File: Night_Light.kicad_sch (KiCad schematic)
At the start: 6 parts, among them J1 3V0, Q1 2N3904

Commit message: Update schematic for KiCad version 7
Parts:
- J1: symbol Connector:Conn_01x02_Male -> Connector:Conn_01x02_Pin

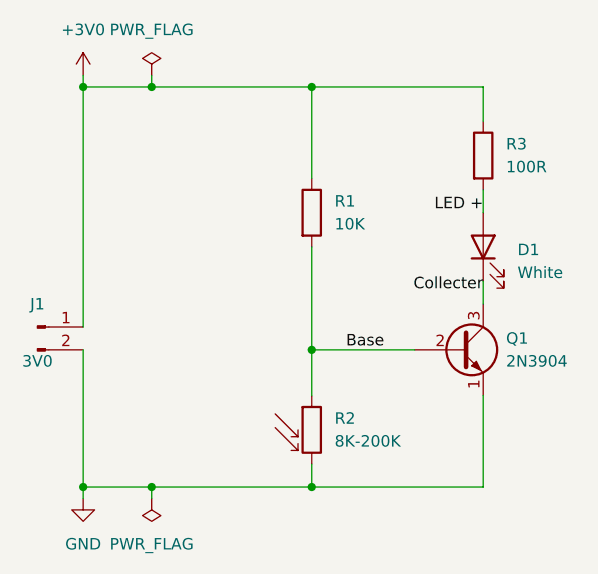
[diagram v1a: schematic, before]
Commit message: Update silkscreen. Fixes #7, #8, #9, and #11
- Change "D1" label to "LED1". #7
- Make silkscreen text bigger and thicker. #8
- Add "+" and "-" to power pads. #9
- Add LED polarity to silkscreen. #11
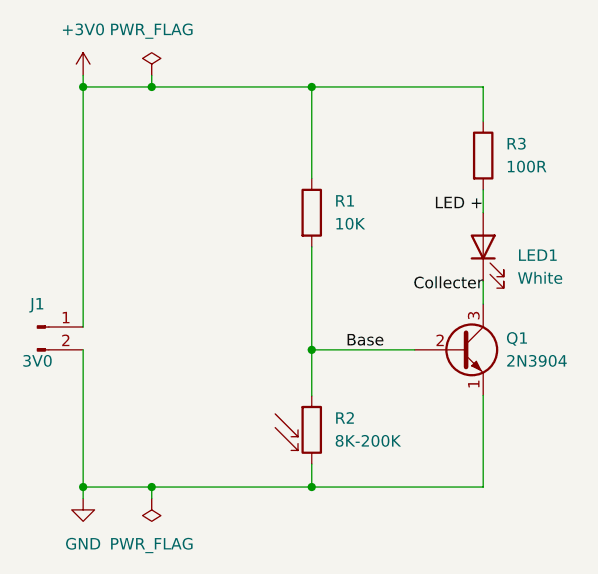
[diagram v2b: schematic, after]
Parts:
- renumbered D1 to LED1
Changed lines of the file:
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@@
   (symbol (lib_id "Device:LED") (at 158.75 93.98 90) (unit 1)
     (in_bom yes) (on_board yes) (dnp no) (fields_autoplaced)
-    (property "Reference" "D1" (at 162.56 94.2974 90)
+    (property "Reference" "LED1" (at 162.56 94.9325 90)
       (effects (font (size 1.27 1.27)) (justify right))
     )
-    (property "Value" "White" (at 162.56 96.8374 90)
+    (property "Value" "White" (at 162.56 97.4725 90)
       (effects (font (size 1.27 1.27)) (justify right))
     )
@@
       (project "Night_Light"
         (path "/92c86926-e096-47bb-9196-37834700b996"
-          (reference "D1") (unit 1)
+          (reference "LED1") (unit 1)
         )
       )

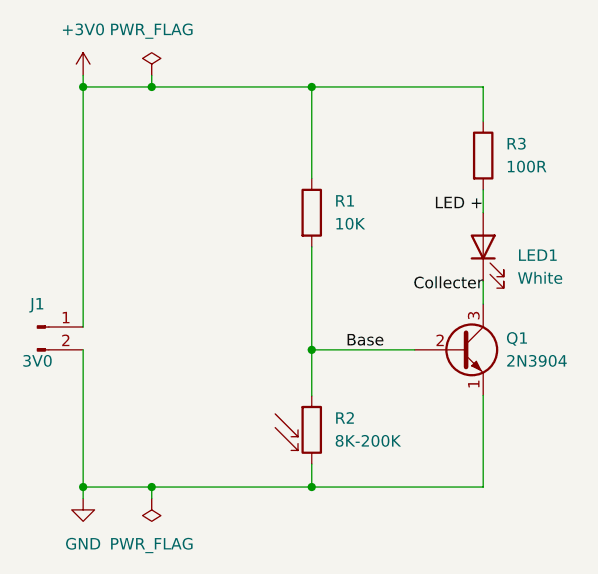
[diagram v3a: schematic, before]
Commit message: Change R3 and add resistor values to silkscreen
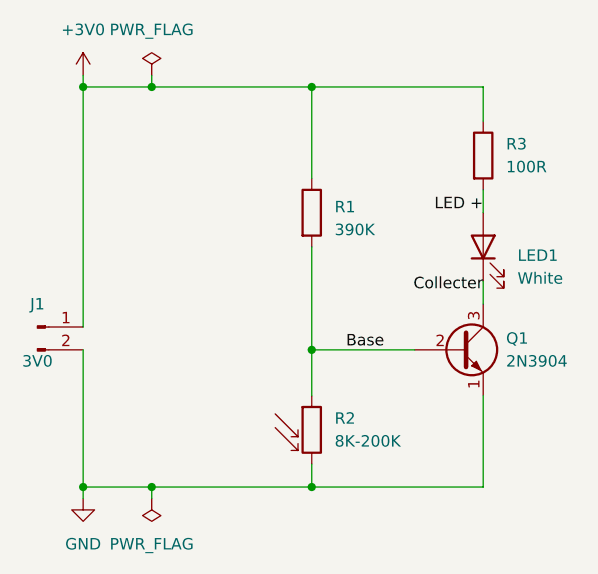
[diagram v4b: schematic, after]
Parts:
- R1: value 10K -> 390K
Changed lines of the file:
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@@
   (symbol (lib_id "Device:R") (at 139.7 90.17 0) (unit 1)
     (in_bom yes) (on_board yes) (dnp no) (fields_autoplaced)
-    (property "Reference" "R1" (at 142.24 88.8999 0)
+    (property "Reference" "R1" (at 142.24 89.535 0)
       (effects (font (size 1.27 1.27)) (justify left))
     )
-    (property "Value" "10K" (at 142.24 91.4399 0)
+    (property "Value" "390K" (at 142.24 92.075 0)
       (effects (font (size 1.27 1.27)) (justify left))
     )
